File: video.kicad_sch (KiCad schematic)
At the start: 4 parts, among them J2 Board Interconnect Female, J2 Video Output Female, J3 Conn_02x08_Odd_Even

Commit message: move to samx4
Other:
- company: (none) -> Dragon Data
- title: (none) -> Dragon 32 CPU UK PAL
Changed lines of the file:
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@@
   (paper "A3")
   (title_block
+    (title "Dragon 32 CPU UK PAL")
     (date "2023-05-25")
     (rev "3.0")
-    (comment 2 "Reposition dram and buffer")
+    (company "Dragon Data")
+    (comment 1 "Modified by Julian Brown")
+    (comment 2 "SAMx4 by Ciaran Anscomb")
   )
   (no_connect (at 167.64 168.91))

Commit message: serial wiring
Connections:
- net +12V: now also PL6.9 (Pin_9); no longer PL6.1 (Pin_1)
- net -5V: no longer PL6.3 (Pin_3)
- net BIAS: now also PL6.1 (Pin_1); no longer PL6.9 (Pin_9)
- net GND: now also PL6.6 (Pin_6); no longer PL6.4 (Pin_4)
- net SOUND: now also PL6.3 (Pin_3); no longer PL6.7 (Pin_7)
- net VID OUT: now also PL6.4 (Pin_4); no longer PL6.6 (Pin_6)
- new net -12V: PL6.7 (Pin_7)
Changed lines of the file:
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@@
     )
   )
-  (global_label "VID OUT" (shape output) (at 202.6412 141.1224 180) (fields_autoplaced)
-    (effects (font (size 1.27 1.27)) (justify right))
-    (property "Intersheetrefs" "${INTERSHEET_REFS}" (at 193.0356 141.1224 0)
+  (global_label "VID OUT" (shape output) (at 202.6412 146.2024 180) (fields_autoplaced)
+    (effects (font (size 1.27 1.27)) (justify right))
+    (property "Intersheetrefs" "${INTERSHEET_REFS}" (at 193.0356 146.2024 0)
       (effects (font (size 1.27 1.27)) (justify right) hide)
     )
@@
     )
   )
-  (global_label "SOUND" (shape input) (at 202.6412 138.5824 180) (fields_autoplaced)
-    (effects (font (size 1.27 1.27)) (justify right))
-    (property "Intersheetrefs" "${INTERSHEET_REFS}" (at 193.9186 138.5824 0)
+  (global_label "SOUND" (shape input) (at 202.6412 148.7424 180) (fields_autoplaced)
+    (effects (font (size 1.27 1.27)) (justify right))
+    (property "Intersheetrefs" "${INTERSHEET_REFS}" (at 193.9186 148.7424 0)
       (effects (font (size 1.27 1.27)) (justify right) hide)
     )
@@
     )
   )
-  (global_label "BIAS" (shape output) (at 202.6412 133.5024 180) (fields_autoplaced)
-    (effects (font (size 1.27 1.27)) (justify right))
-    (property "Intersheetrefs" "${INTERSHEET_REFS}" (at 196.2167 133.5024 0)
+  (global_label "BIAS" (shape output) (at 202.6412 153.8224 180) (fields_autoplaced)
+    (effects (font (size 1.27 1.27)) (justify right))
+    (property "Intersheetrefs" "${INTERSHEET_REFS}" (at 196.2167 153.8224 0)
       (effects (font (size 1.27 1.27)) (justify right) hide)
     )
@@
     )
   )
-  (symbol (lib_id "power:GND") (at 202.6412 146.2024 270) (unit 1)
-    (in_bom yes) (on_board yes) (dnp no) (fields_autoplaced)
-    (property "Reference" "#PWR019" (at 196.2912 146.2024 0)
-      (effects (font (size 1.27 1.27)) hide)
-    )
-    (property "Value" "GND" (at 199.4662 146.2023 90)
+  (symbol (lib_id "power:GND") (at 202.6412 141.1224 270) (mirror x) (unit 1)
+    (in_bom yes) (on_board yes) (dnp no) (fields_autoplaced)
+    (property "Reference" "#PWR019" (at 196.2912 141.1224 0)
+      (effects (font (size 1.27 1.27)) hide)
+    )
+    (property "Value" "GND" (at 199.4662 141.1225 90)
       (effects (font (size 1.27 1.27)) (justify right))
     )
-    (property "Footprint" "" (at 202.6412 146.2024 0)
-      (effects (font (size 1.27 1.27)) hide)
-    )
-    (property "Datasheet" "" (at 202.6412 146.2024 0)
+    (property "Footprint" "" (at 202.6412 141.1224 0)
+      (effects (font (size 1.27 1.27)) hide)
+    )
+    (property "Datasheet" "" (at 202.6412 141.1224 0)
       (effects (font (size 1.27 1.27)) hide)
     )
@@
     )
   )
-  (symbol (lib_id "power:+5V") (at 202.6412 151.2824 90) (unit 1)
+  (symbol (lib_id "power:+5V") (at 202.6412 136.0424 90) (mirror x) (unit 1)
     (in_bom yes) (on_board yes) (dnp no)
-    (property "Reference" "#PWR0281" (at 206.4512 151.2824 0)
-      (effects (font (size 1.27 1.27)) hide)
-    )
-    (property "Value" "+5V" (at 195.6562 151.2824 90)
+    (property "Reference" "#PWR0281" (at 206.4512 136.0424 0)
+      (effects (font (size 1.27 1.27)) hide)
+    )
+    (property "Value" "+5V" (at 195.6562 136.0424 90)
       (effects (font (size 1.27 1.27)) (justify right))
     )
+    (property "Footprint" "" (at 202.6412 136.0424 0)
+      (effects (font (size 1.27 1.27)) hide)
+    )
+    (property "Datasheet" "" (at 202.6412 136.0424 0)
+      (effects (font (size 1.27 1.27)) hide)
+    )
+    (pin "1")
+    (instances
+      (project "Dragon32"
+        (path "/0c3dceba-7c95-4b3d-b590-0eb581444beb/d9dba8db-e731-4cb4-b2de-fefd65b288bc"
+          (reference "#PWR0281") (unit 1)
+        )
+      )
+    )
+  )
+  (symbol (lib_id "power:+5V") (at 202.6412 151.2824 90) (mirror x) (unit 1)
+    (in_bom yes) (on_board yes) (dnp no) (fields_autoplaced)
+    (property "Reference" "#PWR052" (at 206.4512 151.2824 0)
+      (effects (font (size 1.27 1.27)) hide)
+    )
+    (property "Value" "+5V" (at 198.9836 150.6474 90)
+      (effects (font (size 1.27 1.27)) (justify left))
+    )
     (property "Footprint" "" (at 202.6412 151.2824 0)
       (effects (font (size 1.27 1.27)) hide)
     )
     (property "Datasheet" "" (at 202.6412 151.2824 0)
-      (effects (font (size 1.27 1.27)) hide)
-    )
-    (pin "1")
-    (instances
-      (project "Dragon32"
-        (path "/0c3dceba-7c95-4b3d-b590-0eb581444beb/d9dba8db-e731-4cb4-b2de-fefd65b288bc"
-          (reference "#PWR0281") (unit 1)
-        )
-      )
-    )
-  )
-  (symbol (lib_id "power:+5V") (at 202.6412 136.0424 90) (unit 1)
-    (in_bom yes) (on_board yes) (dnp no) (fields_autoplaced)
-    (property "Reference" "#PWR052" (at 206.4512 136.0424 0)
-      (effects (font (size 1.27 1.27)) hide)
-    )
-    (property "Value" "+5V" (at 198.9836 136.6774 90)
-      (effects (font (size 1.27 1.27)) (justify left))
-    )
-    (property "Footprint" "" (at 202.6412 136.0424 0)
-      (effects (font (size 1.27 1.27)) hide)
-    )
-    (property "Datasheet" "" (at 202.6412 136.0424 0)
       (effects (font (size 1.27 1.27)) hide)
     )
@@
     )
   )
+  (symbol (lib_id "power:-12V") (at 202.6412 138.5824 90) (unit 1)
+    (in_bom yes) (on_board yes) (dnp no) (fields_autoplaced)
+    (property "Reference" "#PWR095" (at 200.1012 138.5824 0)
+      (effects (font (size 1.27 1.27)) hide)
+    )
+    (property "Value" "-12V" (at 199.0852 138.5824 90)
+      (effects (font (size 1.27 1.27)) (justify left))
+    )
+    (property "Footprint" "" (at 202.6412 138.5824 0)
+      (effects (font (size 1.27 1.27)) hide)
+    )
+    (property "Datasheet" "" (at 202.6412 138.5824 0)
+      (effects (font (size 1.27 1.27)) hide)
+    )
+    (pin "1")
+    (instances
+      (project "Dragon32"
+        (path "/0c3dceba-7c95-4b3d-b590-0eb581444beb/d9dba8db-e731-4cb4-b2de-fefd65b288bc"
+          (reference "#PWR095") (unit 1)
+        )
+      )
+    )
+  )
   (symbol (lib_id "power:GND") (at 137.1092 167.9448 90) (unit 1)
     (in_bom yes) (on_board yes) (dnp no) (fields_autoplaced)
@@
     )
   )
-  (symbol (lib_id "power:-5V") (at 202.6412 148.7424 90) (unit 1)
-    (in_bom yes) (on_board yes) (dnp no)
-    (property "Reference" "#PWR0282" (at 200.1012 148.7424 0)
-      (effects (font (size 1.27 1.27)) hide)
-    )
-    (property "Value" "-5V" (at 195.5292 148.7424 90)
-      (effects (font (size 1.27 1.27)) (justify right))
-    )
-    (property "Footprint" "" (at 202.6412 148.7424 0)
-      (effects (font (size 1.27 1.27)) hide)
-    )
-    (property "Datasheet" "" (at 202.6412 148.7424 0)
-      (effects (font (size 1.27 1.27)) hide)
-    )
-    (pin "1")
-    (instances
-      (project "Dragon32"
-        (path "/0c3dceba-7c95-4b3d-b590-0eb581444beb/d9dba8db-e731-4cb4-b2de-fefd65b288bc"
-          (reference "#PWR0282") (unit 1)
-        )
-      )
-    )
-  )
-  (symbol (lib_id "power:GND") (at 202.6412 143.6624 270) (unit 1)
+  (symbol (lib_id "power:GND") (at 202.6412 143.6624 270) (mirror x) (unit 1)
     (in_bom yes) (on_board yes) (dnp no) (fields_autoplaced)
     (property "Reference" "#PWR018" (at 196.2912 143.6624 0)
       (effects (font (size 1.27 1.27)) hide)
     )
-    (property "Value" "GND" (at 199.4662 143.6623 90)
+    (property "Value" "GND" (at 199.4662 143.6625 90)
       (effects (font (size 1.27 1.27)) (justify right))
     )
@@
     )
   )
-  (symbol (lib_id "power:+12V") (at 202.6412 153.8224 90) (unit 1)
-    (in_bom yes) (on_board yes) (dnp no) (fields_autoplaced)
-    (property "Reference" "#PWR022" (at 206.4512 153.8224 0)
-      (effects (font (size 1.27 1.27)) hide)
-    )
-    (property "Value" "+12V" (at 199.4662 153.8223 90)
+  (symbol (lib_id "power:+12V") (at 202.6412 133.5024 90) (mirror x) (unit 1)
+    (in_bom yes) (on_board yes) (dnp no) (fields_autoplaced)
+    (property "Reference" "#PWR022" (at 206.4512 133.5024 0)
+      (effects (font (size 1.27 1.27)) hide)
+    )
+    (property "Value" "+12V" (at 199.4662 133.5025 90)
       (effects (font (size 1.27 1.27)) (justify left))
     )
-    (property "Footprint" "" (at 202.6412 153.8224 0)
-      (effects (font (size 1.27 1.27)) hide)
-    )
-    (property "Datasheet" "" (at 202.6412 153.8224 0)
-      (effects (font (size 1.27 1.27)) hide)
-    )
+    (property "Footprint" "" (at 202.6412 133.5024 0)
+      (effects (font (size 1.27 1.27)) hide)
+    )
+    (property "Datasheet" "" (at 202.6412 133.5024 0)
+      (effects (font (size 1.27 1.27)) hide)
+    )

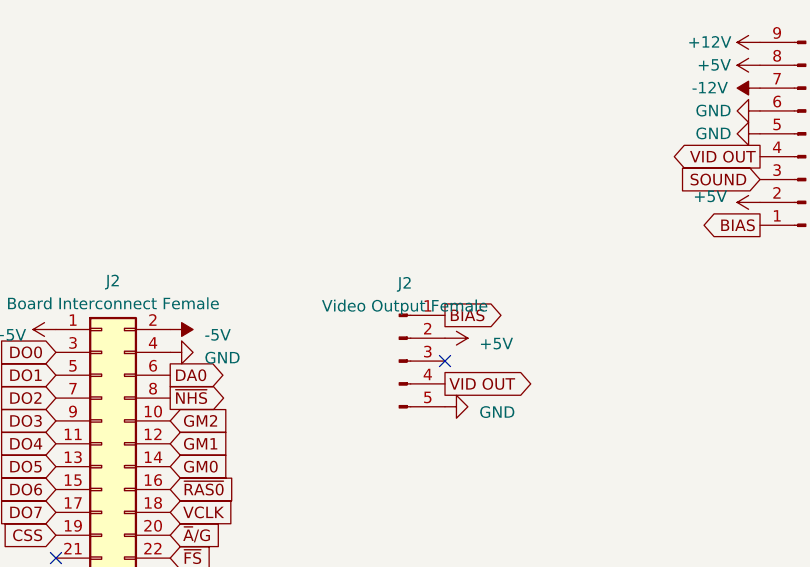
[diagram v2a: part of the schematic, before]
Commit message: fix OE timing on SRAM
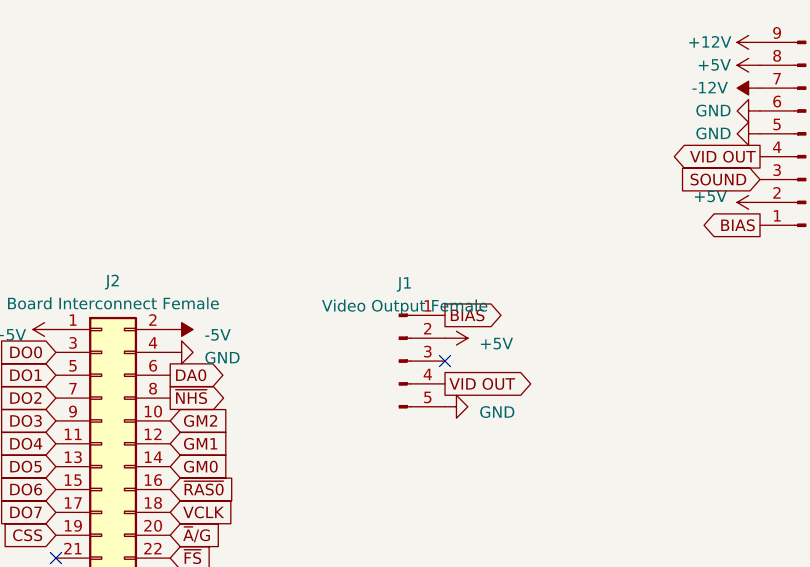
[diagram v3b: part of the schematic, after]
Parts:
- renumbered J2 to J1
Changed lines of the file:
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@@
   (symbol (lib_id "power:+5V") (at 124.4092 165.4048 90) (unit 1)
     (in_bom yes) (on_board yes) (dnp no) (fields_autoplaced)
-    (property "Reference" "#PWR062" (at 128.2192 165.4048 0)
+    (property "Reference" "#PWR04" (at 128.2192 165.4048 0)
       (effects (font (size 1.27 1.27)) hide)
     )
@@
     (instances
       (project "Dragon32"
-        (path "/0c3dceba-7c95-4b3d-b590-0eb581444beb"
-          (reference "#PWR062") (unit 1)
-        )
         (path "/0c3dceba-7c95-4b3d-b590-0eb581444beb/d9dba8db-e731-4cb4-b2de-fefd65b288bc"
           (reference "#PWR04") (unit 1)
@@
   (symbol (lib_id "power:+5V") (at 202.6412 151.2824 90) (mirror x) (unit 1)
     (in_bom yes) (on_board yes) (dnp no) (fields_autoplaced)
-    (property "Reference" "#PWR052" (at 206.4512 151.2824 0)
+    (property "Reference" "#PWR07" (at 206.4512 151.2824 0)
       (effects (font (size 1.27 1.27)) hide)
     )
@@
     (instances
       (project "Dragon32"
-        (path "/0c3dceba-7c95-4b3d-b590-0eb581444beb"
-          (reference "#PWR052") (unit 1)
-        )
         (path "/0c3dceba-7c95-4b3d-b590-0eb581444beb/d9dba8db-e731-4cb4-b2de-fefd65b288bc"
           (reference "#PWR07") (unit 1)
@@
   (symbol (lib_id "power:GND") (at 137.1092 167.9448 90) (unit 1)
     (in_bom yes) (on_board yes) (dnp no) (fields_autoplaced)
-    (property "Reference" "#PWR063" (at 143.4592 167.9448 0)
+    (property "Reference" "#PWR010" (at 143.4592 167.9448 0)
       (effects (font (size 1.27 1.27)) hide)
     )
@@
     (instances
       (project "Dragon32"
-        (path "/0c3dceba-7c95-4b3d-b590-0eb581444beb"
-          (reference "#PWR063") (unit 1)
-        )
         (path "/0c3dceba-7c95-4b3d-b590-0eb581444beb/d9dba8db-e731-4cb4-b2de-fefd65b288bc"
           (reference "#PWR010") (unit 1)
@@
   (symbol (lib_id "Connector:Conn_01x05_Pin") (at 162.56 168.91 0) (unit 1)
     (in_bom yes) (on_board yes) (dnp no) (fields_autoplaced)
-    (property "Reference" "J2" (at 163.195 160.274 0)
+    (property "Reference" "J1" (at 163.195 160.274 0)
       (effects (font (size 1.27 1.27)))
     )
@@
     (instances
       (project "Dragon32"
-        (path "/0c3dceba-7c95-4b3d-b590-0eb581444beb"
-          (reference "J2") (unit 1)
-        )
         (path "/0c3dceba-7c95-4b3d-b590-0eb581444beb/d9dba8db-e731-4cb4-b2de-fefd65b288bc"
           (reference "J1") (unit 1)
@@
   (symbol (lib_id "power:-5V") (at 137.1092 165.4048 270) (unit 1)
     (in_bom yes) (on_board yes) (dnp no) (fields_autoplaced)
-    (property "Reference" "#PWR064" (at 139.6492 165.4048 0)
+    (property "Reference" "#PWR06" (at 139.6492 165.4048 0)
       (effects (font (size 1.27 1.27)) hide)
     )
@@
     (instances
       (project "Dragon32"
-        (path "/0c3dceba-7c95-4b3d-b590-0eb581444beb"
-          (reference "#PWR064") (unit 1)
-        )
         (path "/0c3dceba-7c95-4b3d-b590-0eb581444beb/d9dba8db-e731-4cb4-b2de-fefd65b288bc"
           (reference "#PWR06") (unit 1)
@@
   (symbol (lib_id "power:GND") (at 167.64 173.99 90) (unit 1)
     (in_bom yes) (on_board yes) (dnp no) (fields_autoplaced)
-    (property "Reference" "#PWR053" (at 173.99 173.99 0)
+    (property "Reference" "#PWR050" (at 173.99 173.99 0)
       (effects (font (size 1.27 1.27)) hide)
     )
@@
     (instances
       (project "Dragon32"
-        (path "/0c3dceba-7c95-4b3d-b590-0eb581444beb"
-          (reference "#PWR053") (unit 1)
-        )
         (path "/0c3dceba-7c95-4b3d-b590-0eb581444beb/d9dba8db-e731-4cb4-b2de-fefd65b288bc"
           (reference "#PWR050") (unit 1)
@@
   (symbol (lib_id "power:+5V") (at 167.64 166.37 270) (unit 1)
     (in_bom yes) (on_board yes) (dnp no) (fields_autoplaced)
-    (property "Reference" "#PWR052" (at 163.83 166.37 0)
+    (property "Reference" "#PWR049" (at 163.83 166.37 0)
       (effects (font (size 1.27 1.27)) hide)
     )
@@
     (instances
       (project "Dragon32"
-        (path "/0c3dceba-7c95-4b3d-b590-0eb581444beb"
-          (reference "#PWR052") (unit 1)
-        )
         (path "/0c3dceba-7c95-4b3d-b590-0eb581444beb/d9dba8db-e731-4cb4-b2de-fefd65b288bc"
           (reference "#PWR049") (unit 1)

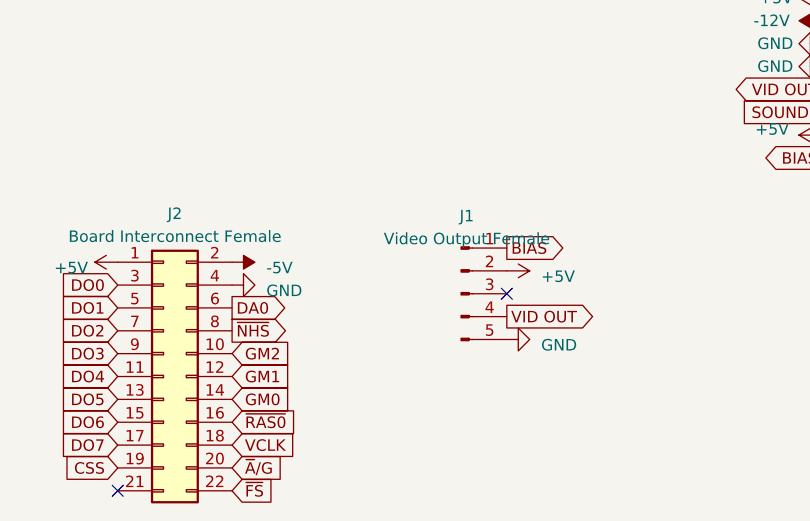
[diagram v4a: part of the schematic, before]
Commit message: move -5v
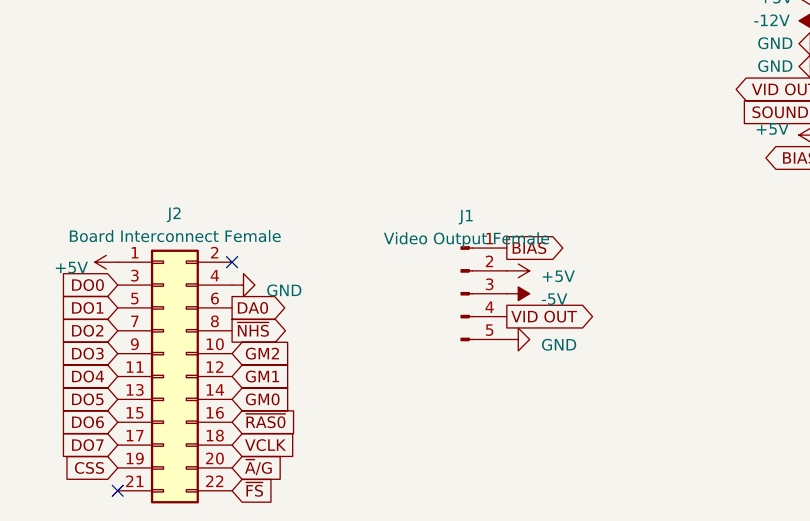
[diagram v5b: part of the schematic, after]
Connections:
- net -5V: now also J1.3 (Pin_3); no longer J2.2 (Pin_2)
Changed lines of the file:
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@@
     (comment 2 "SAMx4 by Ciaran Anscomb")
   )
-  (no_connect (at 167.64 168.91))
   (no_connect (at 123.19 116.84))
+  (no_connect (at 137.1092 165.4048))
   (no_connect (at 123.19 121.92))
   (no_connect (at 123.19 119.38))
@@
     )
   )
+  (symbol (lib_id "power:-5V") (at 167.64 168.91 270) (unit 1)
+    (in_bom yes) (on_board yes) (dnp no) (fields_autoplaced)
+    (property "Reference" "#PWR06" (at 170.18 168.91 0)
+      (effects (font (size 1.27 1.27)) hide)
+    )
+    (property "Value" "-5V" (at 171.45 169.545 90)
+      (effects (font (size 1.27 1.27)) (justify left))
+    )
+    (property "Footprint" "" (at 167.64 168.91 0)
+      (effects (font (size 1.27 1.27)) hide)
+    )
+    (property "Datasheet" "" (at 167.64 168.91 0)
+      (effects (font (size 1.27 1.27)) hide)
+    )
+    (pin "1")
+    (instances
+      (project "Dragon32"
+        (path "/0c3dceba-7c95-4b3d-b590-0eb581444beb/d9dba8db-e731-4cb4-b2de-fefd65b288bc"
+          (reference "#PWR06") (unit 1)
+        )
+      )
+      (project "DragonNTSC"
+        (path "/5c3ccdac-dbfc-47b7-be5c-593b42d2b61c"
+          (reference "#PWR04") (unit 1)
+        )
+      )
+    )
+  )
   (symbol (lib_id "power:-12V") (at 202.6412 138.5824 90) (unit 1)
     (in_bom yes) (on_board yes) (dnp no) (fields_autoplaced)
@@
         )
       )
-    )
-  )
-  (symbol (lib_id "power:-5V") (at 137.1092 165.4048 270) (unit 1)
-    (in_bom yes) (on_board yes) (dnp no) (fields_autoplaced)
-    (property "Reference" "#PWR06" (at 139.6492 165.4048 0)
-      (effects (font (size 1.27 1.27)) hide)
-    )
-    (property "Value" "-5V" (at 140.9192 166.0398 90)
-      (effects (font (size 1.27 1.27)) (justify left))
-    )
-    (property "Footprint" "" (at 137.1092 165.4048 0)
-      (effects (font (size 1.27 1.27)) hide)
-    )
-    (property "Datasheet" "" (at 137.1092 165.4048 0)
-      (effects (font (size 1.27 1.27)) hide)
-    )
-    (pin "1")
-    (instances
-      (project "Dragon32"
-        (path "/0c3dceba-7c95-4b3d-b590-0eb581444beb/d9dba8db-e731-4cb4-b2de-fefd65b288bc"
-          (reference "#PWR06") (unit 1)
-        )
-      )
-      (project "DragonNTSC"
-        (path "/5c3ccdac-dbfc-47b7-be5c-593b42d2b61c"
-          (reference "#PWR04") (unit 1)
-        )
-      )
